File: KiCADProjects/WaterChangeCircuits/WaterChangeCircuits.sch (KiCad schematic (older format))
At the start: 102 parts, among them J1 Conn_01x25, J10 Conn_01x02, J11 Conn_01x02, J12 Conn_01x02, J13 Conn_01x02, J14 Conn_01x02, J15 Conn_01x02, J16 Conn_01x02, J17 Conn_01x02, J18 Conn_01x02, J19 Conn_01x02, J2 Conn_01x27, J20 Conn_01x02, J21 Conn_01x02, J22 Conn_01x02, J23 Conn_01x02, J24 Conn_01x02, J25 Conn_01x02, J26 Conn_01x02, J27 Conn_01x02, J28 Conn_01x02, J29 Conn_01x02, J3 Conn_01x02, J30 Conn_01x02, J31 Conn_01x02, J32 Conn_01x02, J33 Conn_01x02, J34 Conn_01x02, J35 Conn_01x02, J36 Conn_01x02, J37 Conn_01x02, J38 Conn_01x02, J39 Conn_01x02, J4 Conn_01x02, J40 Conn_01x02, J41 Conn_01x02, J42 Conn_01x02, J43 Conn_01x02, J44 Conn_01x02, J45 Conn_01x02, J46 Conn_01x02, J47 Conn_01x02, J48 Conn_01x02, J49 Conn_01x02, J5 Conn_01x02, J50 Conn_01x02, J51 Conn_01x02, J52 Conn_01x02, J53 Conn_01x02, J6 Conn_01x02, J7 Conn_01x02, J8 Conn_01x02, J9 Conn_01x02, U1 TLP3542, U10 TLP3542, U11 TLP3542, U12 TLP3542, U13 TLP3542, U14 TLP3542, U15 TLP3542, U16 TLP3542, U17 TLP3542, U18 TLP3542, U19 TLP3542, U2 TLP3542, U20 TLP3542, U21 TLP3542, U22 TLP3542, U23 TLP3542, U24 TLP3542, U25 TLP3542, U26 TLP3542, U27 TLP3542, U28 TLP3542, U29 TLP3542, U3 TLP3542, U30 TLP3542, U31 TLP3542, U32 TLP3542, U33 TLP3542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

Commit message: Changed the circuit design to make the inputs from the flowmeters digital, started the webform designs for the RPi
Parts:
- removed J10, J11, J12, J13, J14, J15, J16, J17: Conn_01x02, Connector_JST:JST_PH_S2B-PH-K_1x02_P2.00mm_Horizontal, symbol Connector_Generic:Conn_01x02
- removed U10, U11, U12, U13, U6, U7, U8, U9: TLP3542, Package_DIP:DIP-5-6_W7.62mm, symbol Relay_SolidState:TLP3542
- added J?: Conn_01x03, symbol Connector_Generic:Conn_01x03
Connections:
- net T13: no longer J22.1 (Pin_1)
- net T14: no longer J23.1 (Pin_1)
- net T15: no longer J24.1 (Pin_1)
- net T16: no longer J25.1 (Pin_1)
- net T17: no longer J26.1 (Pin_1)
- net T18: no longer J27.1 (Pin_1)
- net T19: no longer J28.1 (Pin_1)
- new net +5V: J?.1 (Pin_1)

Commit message: Completed PCB design and schematics.
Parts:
- removed J2: Conn_01x27, Connector_PinSocket_2.54mm:PinSocket_1x27_P2.54mm_Vertical, symbol Connector_Generic:Conn_01x27
- added H1, H2, H3, H4: MountingHole, MountingHole:MountingHole_3.2mm_M3, symbol Mechanical:MountingHole
- added J11, J13, J14, J15, J16, J17, J74, J75: Conn_01x03, Connector_PinSocket_2.54mm:PinSocket_1x03_P2.54mm_Vertical, symbol Connector_Generic:Conn_01x03
- added J12: Conn_01x12, Connector_PinSocket_2.54mm:PinSocket_1x12_P2.54mm_Vertical, symbol Connector_Generic:Conn_01x12
- added J2: Conn_01x15, Connector_PinSocket_2.54mm:PinSocket_1x15_P2.54mm_Vertical, symbol Connector_Generic:Conn_01x15
- J10: renamed from J?; footprint (none) -> Connector_PinSocket_2.54mm:PinSocket_1x03_P2.54mm_Vertical
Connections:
- net +5V: now also J11.1 (Pin_1), J13.1 (Pin_1), J14.1 (Pin_1), J15.1 (Pin_1), J16.1 (Pin_1), J17.1 (Pin_1), J74.1 (Pin_1), J75.1 (Pin_1)
- net D09: now also J15.2 (Pin_2)
- net D10: now also J14.2 (Pin_2)
- net D11: now also J13.2 (Pin_2)
- net D12: now also J11.2 (Pin_2)
- net D13: now also J10.2 (Pin_2)
- net D14: now also J16.2 (Pin_2)
- net D15: now also J17.2 (Pin_2)
- net D16: now also J74.2 (Pin_2)
- net D17: now also J75.2 (Pin_2)
- net D27: now also J2.15 (Pin_15)
- net D28: now also J2.14 (Pin_14)
- net D29: now also J2.13 (Pin_13)
- net D30: now also J2.12 (Pin_12)
- net D31: now also J2.11 (Pin_11)
- net D32: now also J2.10 (Pin_10)
- net D33: now also J2.9 (Pin_9)
- net D34: now also J2.8 (Pin_8)
- net D35: now also J2.7 (Pin_7)
- net D36: now also J2.6 (Pin_6)
- net D37: now also J2.5 (Pin_5)
- net D38: now also J2.4 (Pin_4)
- net D39: now also J2.3 (Pin_3)
- net D40: now also J2.2 (Pin_2)
- net D41: now also J2.1 (Pin_1)
- net D42: now also J12.12 (Pin_12)
- net D43: now also J12.11 (Pin_11)
- net D44: now also J12.10 (Pin_10)
- net D45: now also J12.9 (Pin_9)
- net D46: now also J12.8 (Pin_8)
- net D47: now also J12.7 (Pin_7)
- net D48: now also J12.6 (Pin_6)
- net D49: now also J12.5 (Pin_5)
- net D50: now also J12.4 (Pin_4)
- net D51: now also J12.3 (Pin_3)
- net D52: now also J12.2 (Pin_2)
- net D53: now also J12.1 (Pin_1)
- net GND2: now also J10.3 (Pin_3), J11.3 (Pin_3), J13.3 (Pin_3), J14.3 (Pin_3), J15.3 (Pin_3), J16.3 (Pin_3), J17.3 (Pin_3), J74.3 (Pin_3), J75.3 (Pin_3)
- net T13: now also J22.1 (Pin_1)
- net T14: now also J23.1 (Pin_1)
- net T15: now also J24.1 (Pin_1)
- net T16: now also J25.1 (Pin_1)
- net T17: now also J26.1 (Pin_1)
- net T18: now also J27.1 (Pin_1)
- net T19: now also J28.1 (Pin_1)
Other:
- moved on the sheet: J5, J6, J7, J8, J9

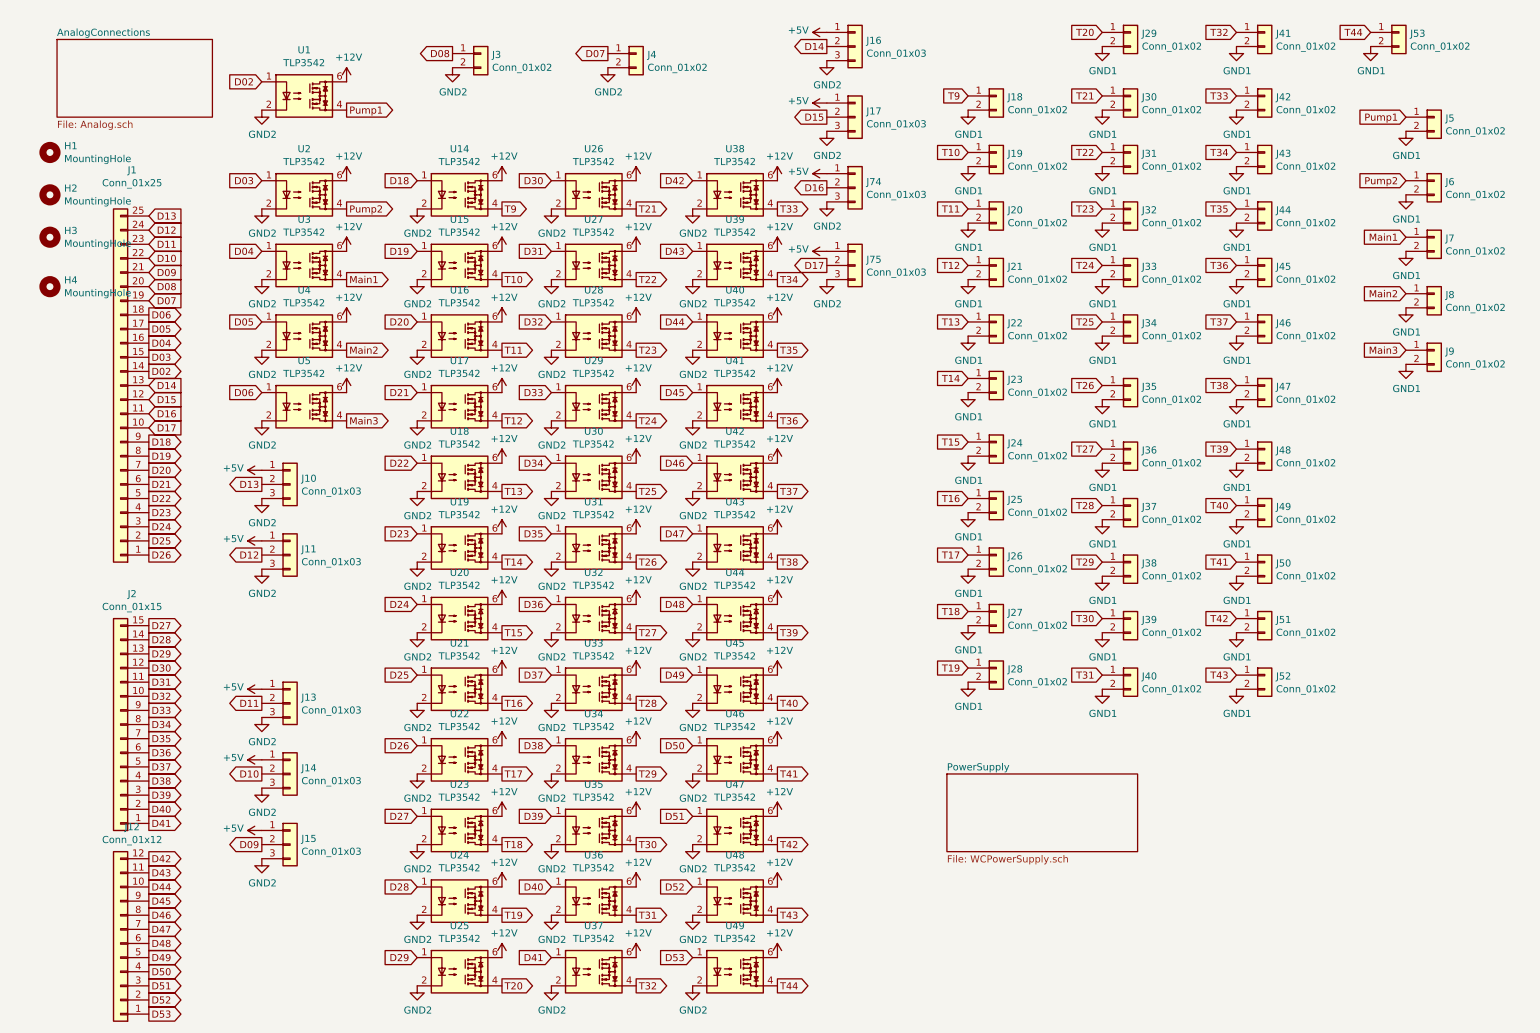
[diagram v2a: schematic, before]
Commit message: Added PDF of the schematic
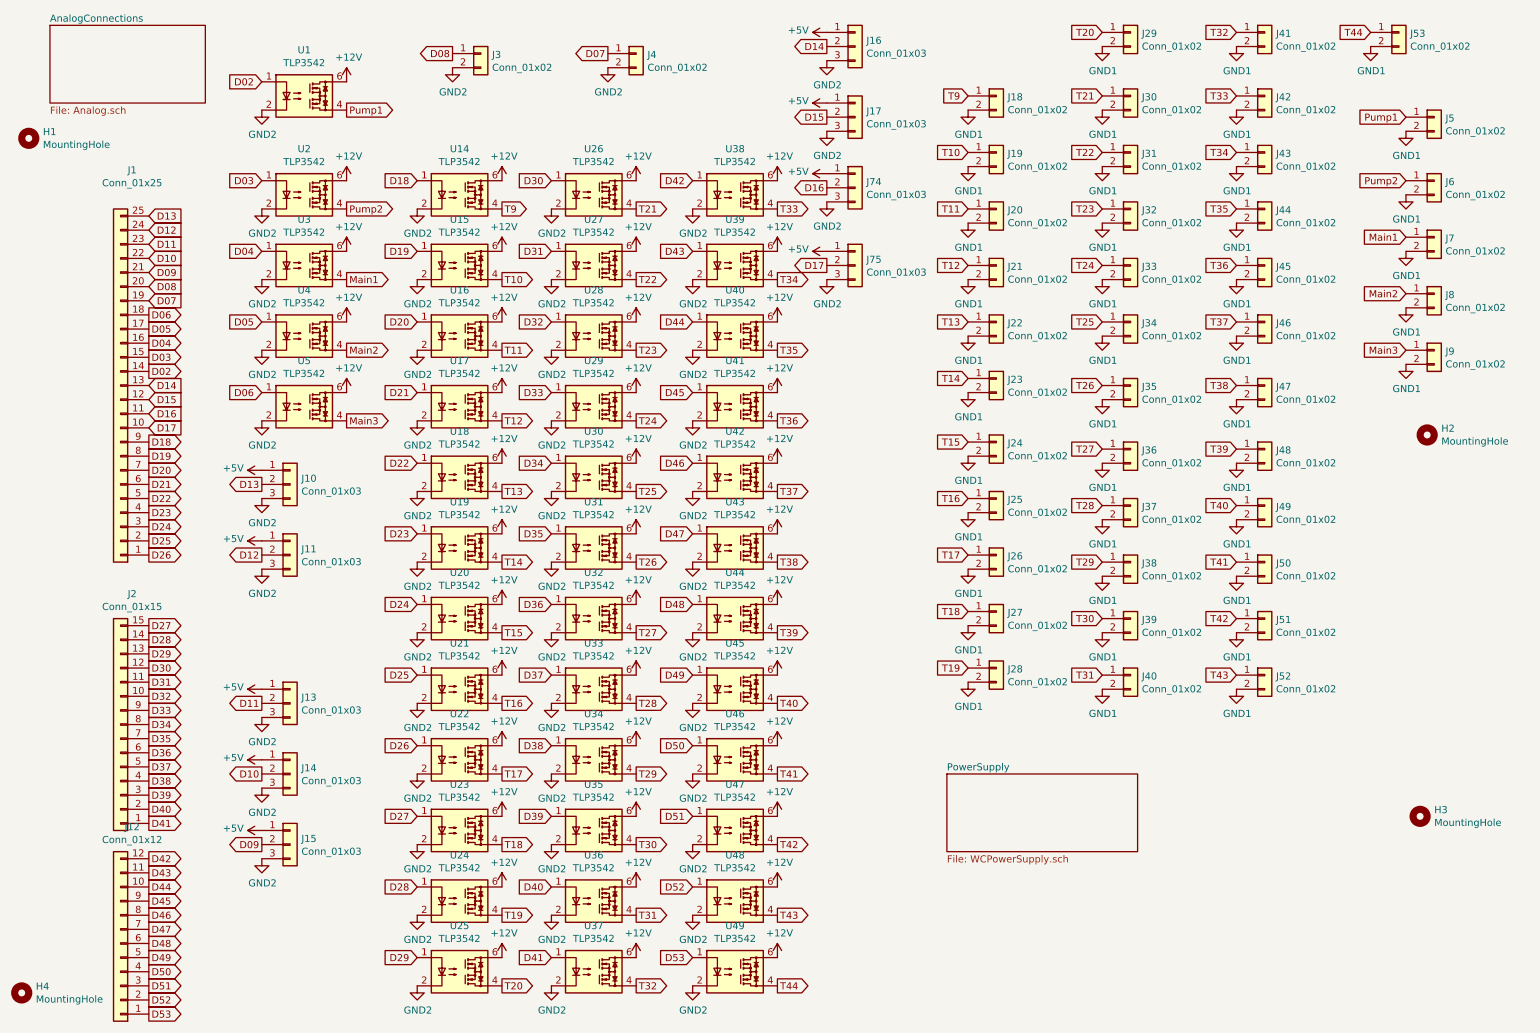
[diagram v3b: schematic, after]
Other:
- moved on the sheet: H1, H2, H3, H4
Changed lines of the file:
@@
 $EndSheet
 $Sheet
-S 850  750  1100 550
+S 800  650  1100 550
 U 60FF9D85
 F0 "AnalogConnections" 50
@@
 L Mechanical:MountingHole H1
 U 1 1 610D4CF8
-P 800 1550
-F 0 "H1" H 900 1596 50  0000 L CNN
-F 1 "MountingHole" H 900 1505 50  0000 L CNN
-F 2 "MountingHole:MountingHole_3.2mm_M3" H 800 1550 50  0001 C CNN
-F 3 "~" H 800 1550 50  0001 C CNN
-	1    800  1550
+P 650 1450
+F 0 "H1" H 750 1496 50  0000 L CNN
+F 1 "MountingHole" H 750 1405 50  0000 L CNN
+F 2 "MountingHole:MountingHole_3.2mm_M3" H 650 1450 50  0001 C CNN
+F 3 "~" H 650 1450 50  0001 C CNN
+	1    650  1450
 	1    0    0    -1
 $EndComp
@@
 L Mechanical:MountingHole H2
 U 1 1 610DEC91
-P 800 1850
-F 0 "H2" H 900 1896 50  0000 L CNN
-F 1 "MountingHole" H 900 1805 50  0000 L CNN
-F 2 "MountingHole:MountingHole_3.2mm_M3" H 800 1850 50  0001 C CNN
-F 3 "~" H 800 1850 50  0001 C CNN
-	1    800  1850
+P 10550 3550
+F 0 "H2" H 10650 3596 50  0000 L CNN
+F 1 "MountingHole" H 10650 3505 50  0000 L CNN
+F 2 "MountingHole:MountingHole_3.2mm_M3" H 10550 3550 50  0001 C CNN
+F 3 "~" H 10550 3550 50  0001 C CNN
+	1    10550 3550
 	1    0    0    -1
 $EndComp
@@
 L Mechanical:MountingHole H3
 U 1 1 610DFA3B
-P 800 2150
-F 0 "H3" H 900 2196 50  0000 L CNN
-F 1 "MountingHole" H 900 2105 50  0000 L CNN
-F 2 "MountingHole:MountingHole_3.2mm_M3" H 800 2150 50  0001 C CNN
-F 3 "~" H 800 2150 50  0001 C CNN
-	1    800  2150
+P 10500 6250
+F 0 "H3" H 10600 6296 50  0000 L CNN
+F 1 "MountingHole" H 10600 6205 50  0000 L CNN
+F 2 "MountingHole:MountingHole_3.2mm_M3" H 10500 6250 50  0001 C CNN
+F 3 "~" H 10500 6250 50  0001 C CNN
+	1    10500 6250
 	1    0    0    -1
 $EndComp
@@
 L Mechanical:MountingHole H4
 U 1 1 610E1423
-P 800 2500
-F 0 "H4" H 900 2546 50  0000 L CNN
-F 1 "MountingHole" H 900 2455 50  0000 L CNN
-F 2 "MountingHole:MountingHole_3.2mm_M3" H 800 2500 50  0001 C CNN
-F 3 "~" H 800 2500 50  0001 C CNN
-	1    800  2500
-	1    0    0    -1
-$EndComp
+P 600 7500
+F 0 "H4" H 700 7546 50  0000 L CNN
+F 1 "MountingHole" H 700 7455 50  0000 L CNN
+F 2 "MountingHole:MountingHole_3.2mm_M3" H 600 7500 50  0001 C CNN
+F 3 "~" H 600 7500 50  0001 C CNN
+	1    600  7500
+	1    0    0    -1
+$EndComp
